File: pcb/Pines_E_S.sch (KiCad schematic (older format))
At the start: 11 parts, among them P1 CONN_01X03, P10 USB_MINI, P11 CONN_02X03, P2 CONN_01X03, P3 CONN_01X03, P4 CONN_01X03, P5 CONN_01X02, P6 CONN_01X02, P7 CONN_01X02, P8 CONN_01X02, P9 CONN_01X02

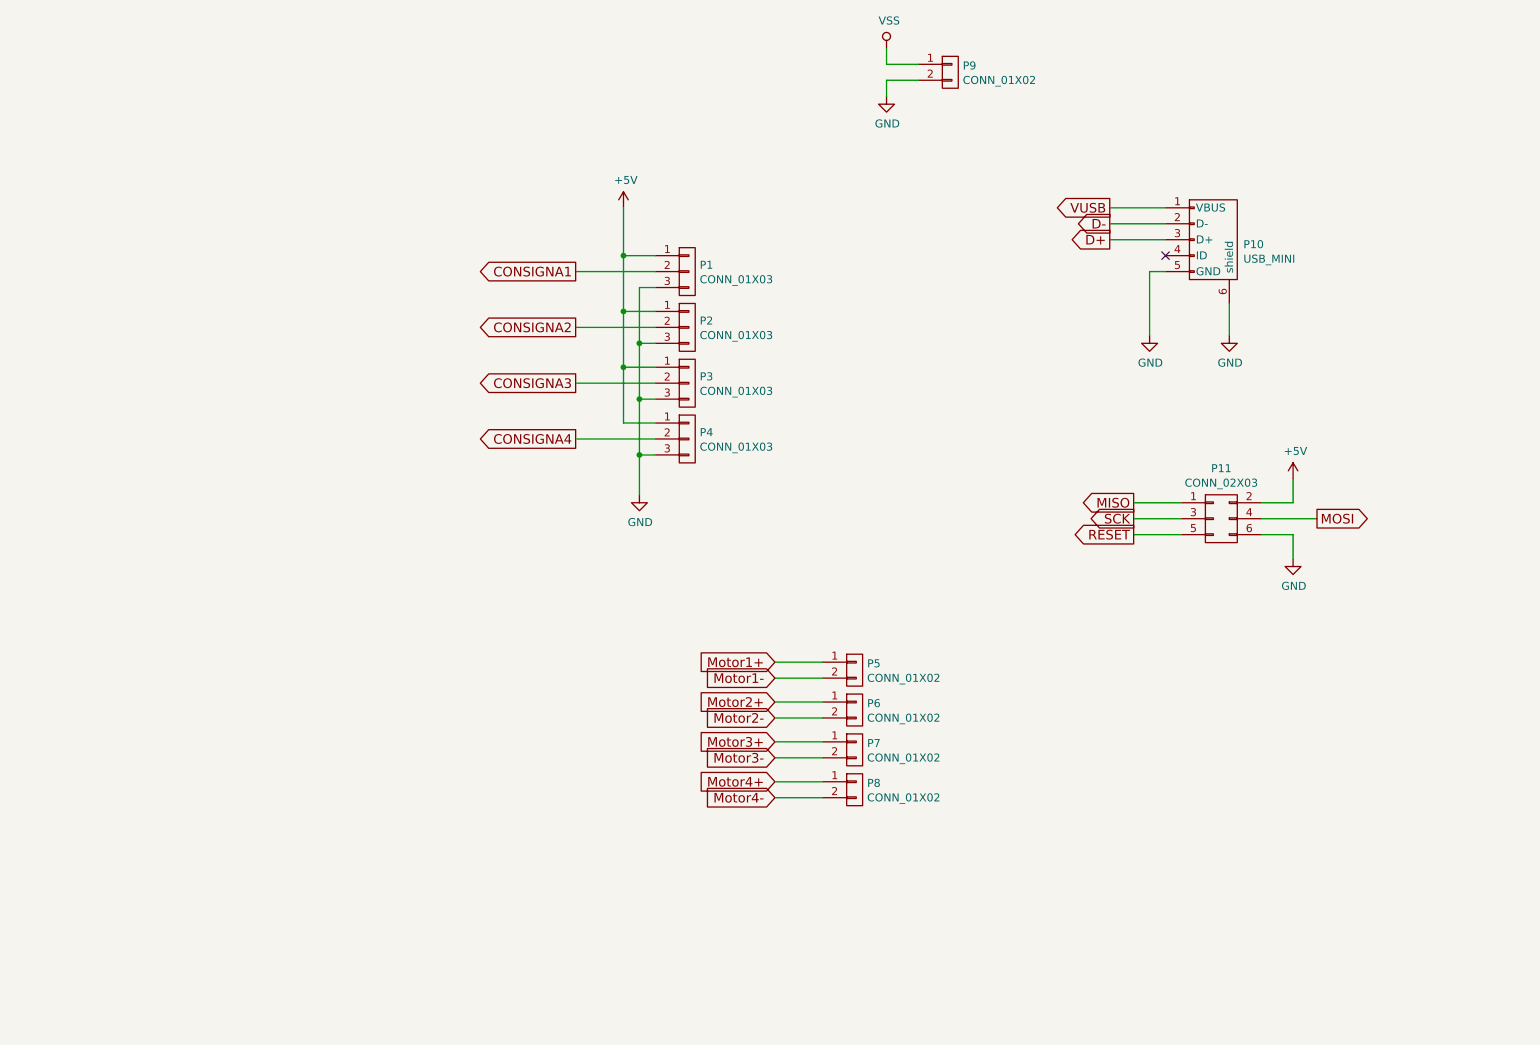
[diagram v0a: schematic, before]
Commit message: carga de hojas jerarquia
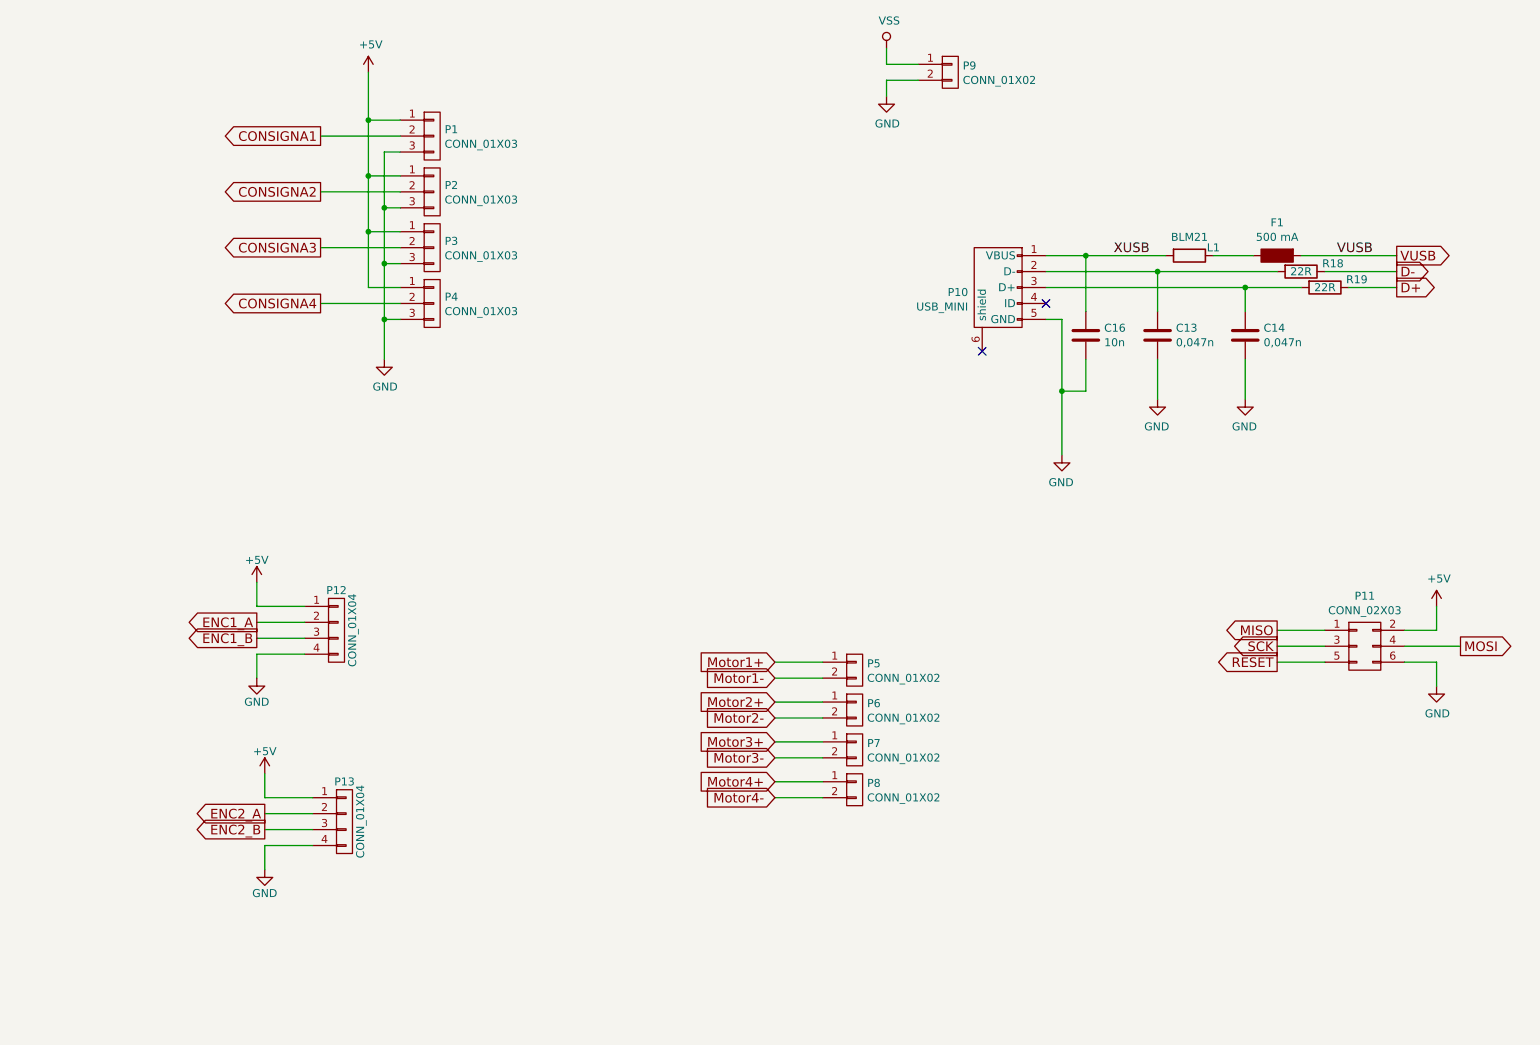
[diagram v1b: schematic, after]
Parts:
- added C13, C14: 0,047n, symbol C
- added C16: 10n, symbol C
- added F1: 500 mA, symbol F
- added L1: BLM21, symbol Ferrita
- added P12, P13: CONN_01X04, symbol CONN_01X04
- added R18, R19: 22R, symbol R
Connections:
- net +5V: now also P12.1 (P1), P13.1 (P1)
- net D+: now also R19.1; no longer P10.3 (D+)
- net D-: now also R18.1; no longer P10.2 (D-)
- net GND: now also C13.2, C14.2, C16.2, P12.4 (P4), P13.4 (P4); no longer P10.6 (shield)
- net VUSB: now also F1.2; no longer P10.1 (VBUS)
- new net: C13.1, P10.2 (D-), R18.2
- new net: C14.1, P10.3 (D+), R19.2
- new net: F1.1, L1.1
- new net ENC1_A: P12.2 (P2)
- new net ENC1_B: P12.3 (P3)
- new net ENC2_A: P13.2 (P2)
- new net ENC2_B: P13.3 (P3)
- new net XUSB: C16.1, L1.2, P10.1 (VBUS)
- no-connect marks 1 -> 2
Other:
- moved on the sheet: P1, P10, P11, P2, P3, P4

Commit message: finalizada realizacion de esquema
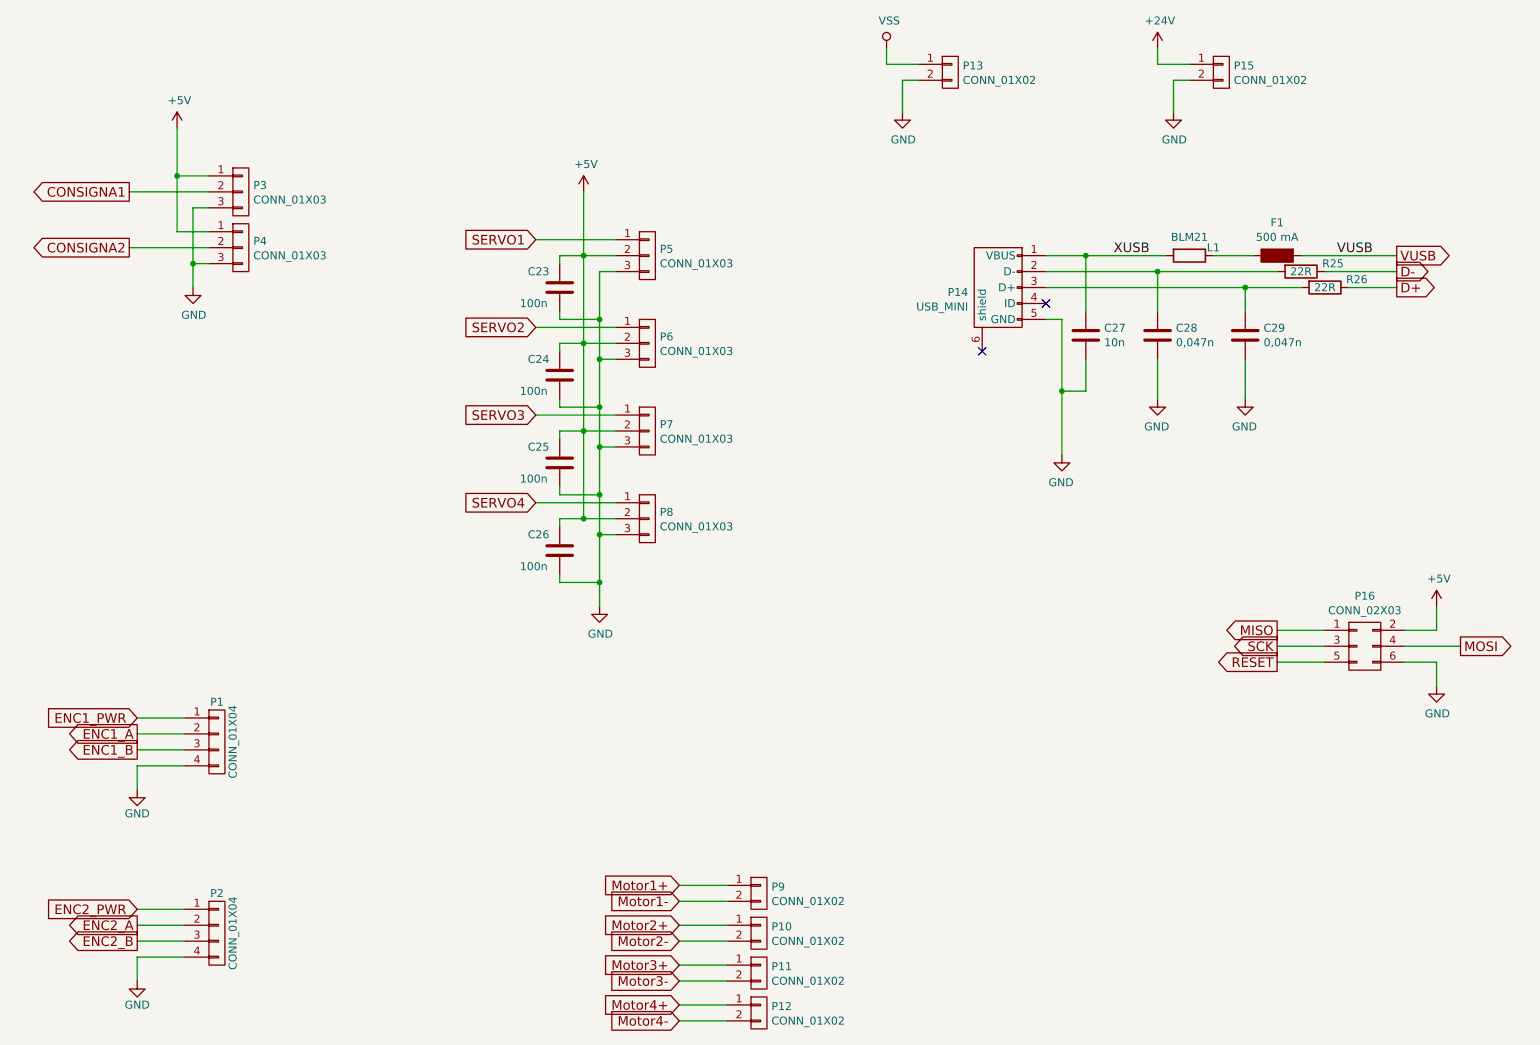
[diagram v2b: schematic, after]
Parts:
- added C23, C24, C25, C26: 100n, symbol C
- added P15: CONN_01X02, symbol CONN_01X02
- added P7, P8: CONN_01X03, symbol CONN_01X03
- renumbered C16 to C27, C13 to C28, C14 to C29, P12 to P1, P6 to P10, P7 to P11, P8 to P12, P9 to P13, P10 to P14, P11 to P16, P13 to P2, P1 to P3, P2 to P4, P3 to P5, P4 to P6, P5 to P9, R18 to R25, R19 to R26
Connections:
- net CONSIGNA3 is gone; now on net +5V: P5.2 (P2)
- net CONSIGNA4 is gone; now on net +5V: P6.2 (P2)
- net +5V: now also C23.1, C24.1, C25.1, C26.1, P7.2 (P2), P8.2 (P2); no longer P1.1 (P1), P2.1 (P1), P5.1 (P1), P6.1 (P1)
- net GND: now also C23.2, C24.2, C25.2, C26.2, P15.2 (P2), P7.3 (P3), P8.3 (P3)
- new net +24V: P15.1 (P1)
- new net ENC1_PWR: P1.1 (P1)
- new net ENC2_PWR: P2.1 (P1)
- new net SERVO1: P5.1 (P1)
- new net SERVO2: P6.1 (P1)
- new net SERVO3: P7.1 (P1)
- new net SERVO4: P8.1 (P1)
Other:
- moved on the sheet: P1, P10, P11, P12, P2, P3, P4, P5, P6, P9

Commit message: asociacion de huellas a resistencias y condensadores
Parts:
- C23, C24, C25, C26: footprint (none) -> Capacitors_SMD:C_0805
- C27: footprint (none) -> Capacitors_SMD:C_0805; Fabricante (none) -> SAMSUNG; Provedor (none) -> tme; Ref (none) -> CL21B103JBANNNC; Ref_Proveedor (none) -> CL21B103JBANNNC
- C28: footprint (none) -> Capacitors_SMD:C_0805; Fabricante (none) -> SAMSUNG; Provedor (none) -> tme; Ref (none) -> CL21C470JBANNNC; Ref_Proveedor (none) -> CL21C470JBANNNC
- C29: footprint (none) -> Capacitors_SMD:C_0805; Provedor (none) -> tme; Ref (none) -> CL21C470JBANNNC; Ref_Proveedor (none) -> CL21C470JBANNNC
- R25, R26: footprint (none) -> Resistors_SMD:R_0805; Fabricante (none) -> VISHAY; Provedor (none) -> tme; Ref (none) -> CRCW080522R0FKEA; Ref_Proveedor (none) -> CRCW080522R0FKEA
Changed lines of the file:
@@
 F 0 "P16" H 9500 5115 50  0000 C CNN
 F 1 "CONN_02X03" H 9500 5024 50  0000 C CNN
-F 2 "" H 9500 3600 50  0000 C CNN
+F 2 "" H 9500 3600 50  0001 C CNN
 F 3 "" H 9500 3600 50  0000 C CNN
 F 4 "~" H 2100 2900 60  0001 C CNN "Fabricante"
@@
 F 0 "P14" V 7230 2738 50  0000 L CNN
 F 1 "USB_MINI" V 7321 2738 50  0000 L CNN
-F 2 "" V 7150 2450 50  0000 C CNN
+F 2 "" V 7150 2450 50  0001 C CNN
 F 3 "" V 7150 2450 50  0000 C CNN
 F 4 "~" H -150 2400 60  0001 C CNN "Fabricante"
@@
 F 0 "P9" H 5778 6391 50  0000 L CNN
 F 1 "CONN_01X02" H 5778 6300 50  0000 L CNN
-F 2 "" H 5700 6350 50  0000 C CNN
+F 2 "" H 5700 6350 50  0001 C CNN
 F 3 "" H 5700 6350 50  0000 C CNN
 F 4 "~" H 1600 3400 60  0001 C CNN "Fabricante"
@@
 F 0 "P10" H 5778 6641 50  0000 L CNN
 F 1 "CONN_01X02" H 5778 6550 50  0000 L CNN
-F 2 "" H 5700 6600 50  0000 C CNN
+F 2 "" H 5700 6600 50  0001 C CNN
 F 3 "" H 5700 6600 50  0000 C CNN
 F 4 "~" H 1600 3400 60  0001 C CNN "Fabricante"
@@
 F 0 "P11" H 5778 6891 50  0000 L CNN
 F 1 "CONN_01X02" H 5778 6800 50  0000 L CNN
-F 2 "" H 5700 6850 50  0000 C CNN
+F 2 "" H 5700 6850 50  0001 C CNN
 F 3 "" H 5700 6850 50  0000 C CNN
 F 4 "~" H 1600 3400 60  0001 C CNN "Fabricante"
@@
 F 0 "P12" H 5778 7141 50  0000 L CNN
 F 1 "CONN_01X02" H 5778 7050 50  0000 L CNN
-F 2 "" H 5700 7100 50  0000 C CNN
+F 2 "" H 5700 7100 50  0001 C CNN
 F 3 "" H 5700 7100 50  0000 C CNN
 F 4 "~" H 1600 3400 60  0001 C CNN "Fabricante"
@@
 F 0 "P3" H 2528 1991 50  0000 L CNN
 F 1 "CONN_01X03" H 2528 1900 50  0000 L CNN
-F 2 "" H 2450 1950 50  0000 C CNN
+F 2 "" H 2450 1950 50  0001 C CNN
 F 3 "" H 2450 1950 50  0000 C CNN
 F 4 "~" H 1000 2350 60  0001 C CNN "Fabricante"
@@
 F 0 "P4" H 2528 2341 50  0000 L CNN
 F 1 "CONN_01X03" H 2528 2250 50  0000 L CNN
-F 2 "" H 2450 2300 50  0000 C CNN
+F 2 "" H 2450 2300 50  0001 C CNN
 F 3 "" H 2450 2300 50  0000 C CNN
 F 4 "~" H 1000 2350 60  0001 C CNN "Fabricante"
@@
 F 0 "P5" H 5078 2391 50  0000 L CNN
 F 1 "CONN_01X03" H 5078 2300 50  0000 L CNN
-F 2 "" H 5000 2350 50  0000 C CNN
+F 2 "" H 5000 2350 50  0001 C CNN
 F 3 "" H 5000 2350 50  0000 C CNN
 F 4 "~" H 3550 2050 60  0001 C CNN "Fabricante"
@@
 F 0 "P6" H 5078 2941 50  0000 L CNN
 F 1 "CONN_01X03" H 5078 2850 50  0000 L CNN
-F 2 "" H 5000 2900 50  0000 C CNN
+F 2 "" H 5000 2900 50  0001 C CNN
 F 3 "" H 5000 2900 50  0000 C CNN
 F 4 "~" H 3550 2250 60  0001 C CNN "Fabricante"
@@
 F 0 "P13" H 6978 1241 50  0000 L CNN
 F 1 "CONN_01X02" H 6978 1150 50  0000 L CNN
-F 2 "" H 6900 1200 50  0000 C CNN
+F 2 "" H 6900 1200 50  0001 C CNN
 F 3 "" H 6900 1200 50  0000 C CNN
 F 4 "~" H 2200 2000 60  0001 C CNN "Fabricante"
@@
 F 0 "P1" H 2300 5650 50  0000 C CNN
 F 1 "CONN_01X04" V 2400 5400 50  0000 C CNN
-F 2 "" H 2300 5400 50  0000 C CNN
+F 2 "" H 2300 5400 50  0001 C CNN
 F 3 "" H 2300 5400 50  0000 C CNN
 F 4 "~" H 1450 2700 60  0001 C CNN "Fabricante"
@@
 F 0 "P2" H 2300 6850 50  0000 C CNN
 F 1 "CONN_01X04" V 2400 6600 50  0000 C CNN
-F 2 "" H 2300 6600 50  0000 C CNN
+F 2 "" H 2300 6600 50  0001 C CNN
 F 3 "" H 2300 6600 50  0000 C CNN
 F 4 "~" H 1400 2700 60  0001 C CNN "Fabricante"
@@
 F 0 "F1" V 8743 2350 50  0000 C CNN
 F 1 "500 mA" V 8834 2350 50  0000 C CNN
-F 2 "" V 8880 2350 50  0000 C CNN
+F 2 "" V 8880 2350 50  0001 C CNN
 F 3 "" H 8950 2350 50  0000 C CNN
 F 4 "ece" H 8950 2350 60  0001 C CNN "Fabricante"
@@
 F 0 "R25" V 9050 2650 50  0000 C CNN
 F 1 "22R" V 9100 2450 50  0000 C CNN
-F 2 "" V 9030 2450 50  0000 C CNN
+F 2 "Resistors_SMD:R_0805" V 9030 2450 50  0001 C CNN
 F 3 "" H 9100 2450 50  0000 C CNN
+F 4 "VISHAY" H 9100 2450 60  0001 C CNN "Fabricante"
+F 5 "CRCW080522R0FKEA" H 9100 2450 60  0001 C CNN "Ref"
+F 6 "~" H 9100 2450 60  0001 C CNN "Potencia"
+F 7 "~" H 9100 2450 60  0001 C CNN "Tolerancia"
+F 8 "tme" H 9100 2450 60  0001 C CNN "Provedor"
+F 9 "CRCW080522R0FKEA" H 9100 2450 60  0001 C CNN "Ref_Proveedor"
 	1    9100 2450
 	0    1    1    0
@@
 F 0 "R26" V 9200 2750 50  0000 C CNN
 F 1 "22R" V 9250 2550 50  0000 C CNN
-F 2 "" V 9180 2550 50  0000 C CNN
+F 2 "Resistors_SMD:R_0805" V 9180 2550 50  0001 C CNN
 F 3 "" H 9250 2550 50  0000 C CNN
+F 4 "VISHAY" H 9250 2550 60  0001 C CNN "Fabricante"
+F 5 "CRCW080522R0FKEA" H 9250 2550 60  0001 C CNN "Ref"
+F 6 "~" H 9250 2550 60  0001 C CNN "Potencia"
+F 7 "~" H 9250 2550 60  0001 C CNN "Tolerancia"
+F 8 "tme" H 9250 2550 60  0001 C CNN "Provedor"
+F 9 "CRCW080522R0FKEA" H 9250 2550 60  0001 C CNN "Ref_Proveedor"
 	1    9250 2550
 	0    1    1    0
@@
 F 0 "L1" V 8350 2500 50  0000 C CNN
 F 1 "BLM21" V 8284 2350 50  0000 C CNN
-F 2 "" V 8330 2350 50  0000 C CNN
+F 2 "" V 8330 2350 50  0001 C CNN
 F 3 "" H 8400 2350 50  0000 C CNN
 F 4 "Murata" H 8400 2350 60  0001 C CNN "Fabricante"
@@
 F 0 "C28" H 8315 2896 50  0000 L CNN
 F 1 "0,047n" H 8315 2805 50  0000 L CNN
-F 2 "" H 8238 2700 50  0000 C CNN
+F 2 "Capacitors_SMD:C_0805" H 8238 2700 50  0001 C CNN
 F 3 "" H 8200 2850 50  0000 C CNN
-F 4 "~" H 8200 2850 60  0001 C CNN "Fabricante"
-F 5 "~" H 8200 2850 60  0001 C CNN "Ref"
+F 4 "SAMSUNG" H 8200 2850 60  0001 C CNN "Fabricante"
+F 5 "CL21C470JBANNNC" H 8200 2850 60  0001 C CNN "Ref"
 F 6 "~" H 8200 2850 60  0001 C CNN "Potencia"
 F 7 "~" H 8200 2850 60  0001 C CNN "Tolerancia"
-F 8 "~" H 8200 2850 60  0001 C CNN "Provedor"
-F 9 "~" H 8200 2850 60  0001 C CNN "Ref_Proveedor"
+F 8 "tme" H 8200 2850 60  0001 C CNN "Provedor"
+F 9 "CL21C470JBANNNC" H 8200 2850 60  0001 C CNN "Ref_Proveedor"
 	1    8200 2850
 	1    0    0    -1
@@
 F 0 "C29" H 8865 2896 50  0000 L CNN
 F 1 "0,047n" H 8865 2805 50  0000 L CNN
-F 2 "" H 8788 2700 50  0000 C CNN
+F 2 "Capacitors_SMD:C_0805" H 8788 2700 50  0001 C CNN
 F 3 "" H 8750 2850 50  0000 C CNN
 F 4 "~" H 8750 2850 60  0001 C CNN "Fabricante"
-F 5 "~" H 8750 2850 60  0001 C CNN "Ref"
+F 5 "CL21C470JBANNNC" H 8750 2850 60  0001 C CNN "Ref"
 F 6 "~" H 8750 2850 60  0001 C CNN "Potencia"
 F 7 "~" H 8750 2850 60  0001 C CNN "Tolerancia"
-F 8 "~" H 8750 2850 60  0001 C CNN "Provedor"
-F 9 "~" H 8750 2850 60  0001 C CNN "Ref_Proveedor"
+F 8 "tme" H 8750 2850 60  0001 C CNN "Provedor"
+F 9 "CL21C470JBANNNC" H 8750 2850 60  0001 C CNN "Ref_Proveedor"
 	1    8750 2850
 	1    0    0    -1
@@
 F 0 "C27" H 7865 2896 50  0000 L CNN
 F 1 "10n" H 7865 2805 50  0000 L CNN
-F 2 "" H 7788 2700 50  0000 C CNN
+F 2 "Capacitors_SMD:C_0805" H 7788 2700 50  0001 C CNN
 F 3 "" H 7750 2850 50  0000 C CNN
-F 4 "~" H 7750 2850 60  0001 C CNN "Fabricante"
-F 5 "~" H 7750 2850 60  0001 C CNN "Ref"
+F 4 "SAMSUNG" H 7750 2850 60  0001 C CNN "Fabricante"
+F 5 "CL21B103JBANNNC" H 7750 2850 60  0001 C CNN "Ref"
 F 6 "~" H 7750 2850 60  0001 C CNN "Potencia"
 F 7 "~" H 7750 2850 60  0001 C CNN "Tolerancia"
-F 8 "~" H 7750 2850 60  0001 C CNN "Provedor"
-F 9 "~" H 7750 2850 60  0001 C CNN "Ref_Proveedor"
+F 8 "tme" H 7750 2850 60  0001 C CNN "Provedor"
+F 9 "CL21B103JBANNNC" H 7750 2850 60  0001 C CNN "Ref_Proveedor"
 	1    7750 2850
 	1    0    0    -1
@@
 F 0 "P7" H 5078 3491 50  0000 L CNN
 F 1 "CONN_01X03" H 5078 3400 50  0000 L CNN
-F 2 "" H 5000 3450 50  0000 C CNN
+F 2 "" H 5000 3450 50  0001 C CNN
 F 3 "" H 5000 3450 50  0000 C CNN
 F 4 "~" H 3550 3150 60  0001 C CNN "Fabricante"
@@
 F 0 "P8" H 5078 4041 50  0000 L CNN
 F 1 "CONN_01X03" H 5078 3950 50  0000 L CNN
-F 2 "" H 5000 4000 50  0000 C CNN
+F 2 "" H 5000 4000 50  0001 C CNN
 F 3 "" H 5000 4000 50  0000 C CNN
 F 4 "~" H 3550 3350 60  0001 C CNN "Fabricante"
@@
 F 0 "C23" H 4250 2650 50  0000 L CNN
 F 1 "100n" H 4200 2450 50  0000 L CNN
-F 2 "" H 4488 2400 50  0000 C CNN
+F 2 "Capacitors_SMD:C_0805" H 4488 2400 50  0001 C CNN
 F 3 "" H 4450 2550 50  0000 C CNN
 F 4 "~" H 4450 2550 60  0001 C CNN "Fabricante"
@@
 F 0 "C24" H 4250 3200 50  0000 L CNN
 F 1 "100n" H 4200 3000 50  0000 L CNN
-F 2 "" H 4488 2950 50  0000 C CNN
+F 2 "Capacitors_SMD:C_0805" H 4488 2950 50  0001 C CNN
 F 3 "" H 4450 3100 50  0000 C CNN
 F 4 "~" H 4450 3100 60  0001 C CNN "Fabricante"
@@
 F 0 "C25" H 4250 3750 50  0000 L CNN
 F 1 "100n" H 4200 3550 50  0000 L CNN
-F 2 "" H 4488 3500 50  0000 C CNN
+F 2 "Capacitors_SMD:C_0805" H 4488 3500 50  0001 C CNN
 F 3 "" H 4450 3650 50  0000 C CNN
 F 4 "~" H 4450 3650 60  0001 C CNN "Fabricante"
@@
 F 0 "C26" H 4250 4300 50  0000 L CNN
 F 1 "100n" H 4200 4100 50  0000 L CNN
-F 2 "" H 4488 4050 50  0000 C CNN
+F 2 "Capacitors_SMD:C_0805" H 4488 4050 50  0001 C CNN
 F 3 "" H 4450 4200 50  0000 C CNN
 F 4 "~" H 4450 4200 60  0001 C CNN "Fabricante"
@@
 F 0 "P15" H 8678 1241 50  0000 L CNN
 F 1 "CONN_01X02" H 8678 1150 50  0000 L CNN
-F 2 "" H 8600 1200 50  0000 C CNN
+F 2 "" H 8600 1200 50  0001 C CNN
 F 3 "" H 8600 1200 50  0000 C CNN
 F 4 "~" H 3900 2000 60  0001 C CNN "Fabricante"

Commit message: añadidas asociaciones de condensadores y led
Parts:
- P14: footprint (none) -> Conectores:usb_mini_molex_675031020
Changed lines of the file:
@@
 F 0 "P14" V 7230 2738 50  0000 L CNN
 F 1 "USB_MINI" V 7321 2738 50  0000 L CNN
-F 2 "" V 7150 2450 50  0001 C CNN
+F 2 "Conectores:usb_mini_molex_675031020" V 7150 2450 50  0001 C CNN
 F 3 "" V 7150 2450 50  0000 C CNN
 F 4 "~" H -150 2400 60  0001 C CNN "Fabricante"
